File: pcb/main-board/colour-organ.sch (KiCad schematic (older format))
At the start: 39 parts, among them U4 LM358_BIG, U5 LM358_BIG

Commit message: working on finding components for parts
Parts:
- R13: renamed from R19; value 15k -> 18k
- R14: renamed from R23; value 3.9k -> 8.2k
- R15: renamed from R20; value 15k -> 18k
- R16: renamed from R28; value 8.2k -> 18k
- R19: renamed from R24; value 10k -> 2.2k
- R20: renamed from R26; value 680R -> 180R
- R21: renamed from R12; value 15k -> 18k
- R22: renamed from R17; value 10k -> 2.2k
- R23: renamed from R22; value 680R -> 180R
- R24: renamed from R25; value 100k -> 22k
- R25: renamed from R18; value 100k -> 22k
- R26: renamed from R13; value 15k -> 18k
- R29: renamed from R10; value 10k -> 2.2k
- R30: renamed from R14; value 680R -> 180R
- R31: renamed from R11; value 100k -> 22k
- renumbered C25 to C14, C16 to C15, C26 to C16, C20 to C17, C17 to C18, C23 to C19, C24 to C20, C14 to C22, C27 to C23, C19 to C24, C22 to C25, C15 to C26, C18 to C27, D3 to D1, D1 to D3, R9 to R17, R16 to R18, R21 to R28, R15 to R32, U5 to U4, U4 to U5
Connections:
- net at C19.1, R15.2: now also U4.5 (NON_INV); no longer U4.3 (NON_INV)
- net at C17.1, C21.2: now also U4.6 (INV), U4.7 (OUT); no longer U4.1 (OUT), U4.2 (INV)
- net at C20.2, R14.2: now also U4.1 (OUT), U4.2 (INV); no longer U4.6 (INV), U4.7 (OUT)
- net at C16.1, R16.2: now also U4.3 (NON_INV); no longer U4.5 (NON_INV)
- net at R17.2, R21.1: now also U5.1 (OUT), U5.2 (INV); no longer U5.6 (INV), U5.7 (OUT)
- net at C18.1, R18.2: now also U5.3 (NON_INV); no longer U5.5 (NON_INV)
- net at C24.1, R26.2: now also U5.5 (NON_INV); no longer U5.3 (NON_INV)
- net at C22.1, C26.2: now also U5.6 (INV), U5.7 (OUT); no longer U5.1 (OUT), U5.2 (INV)

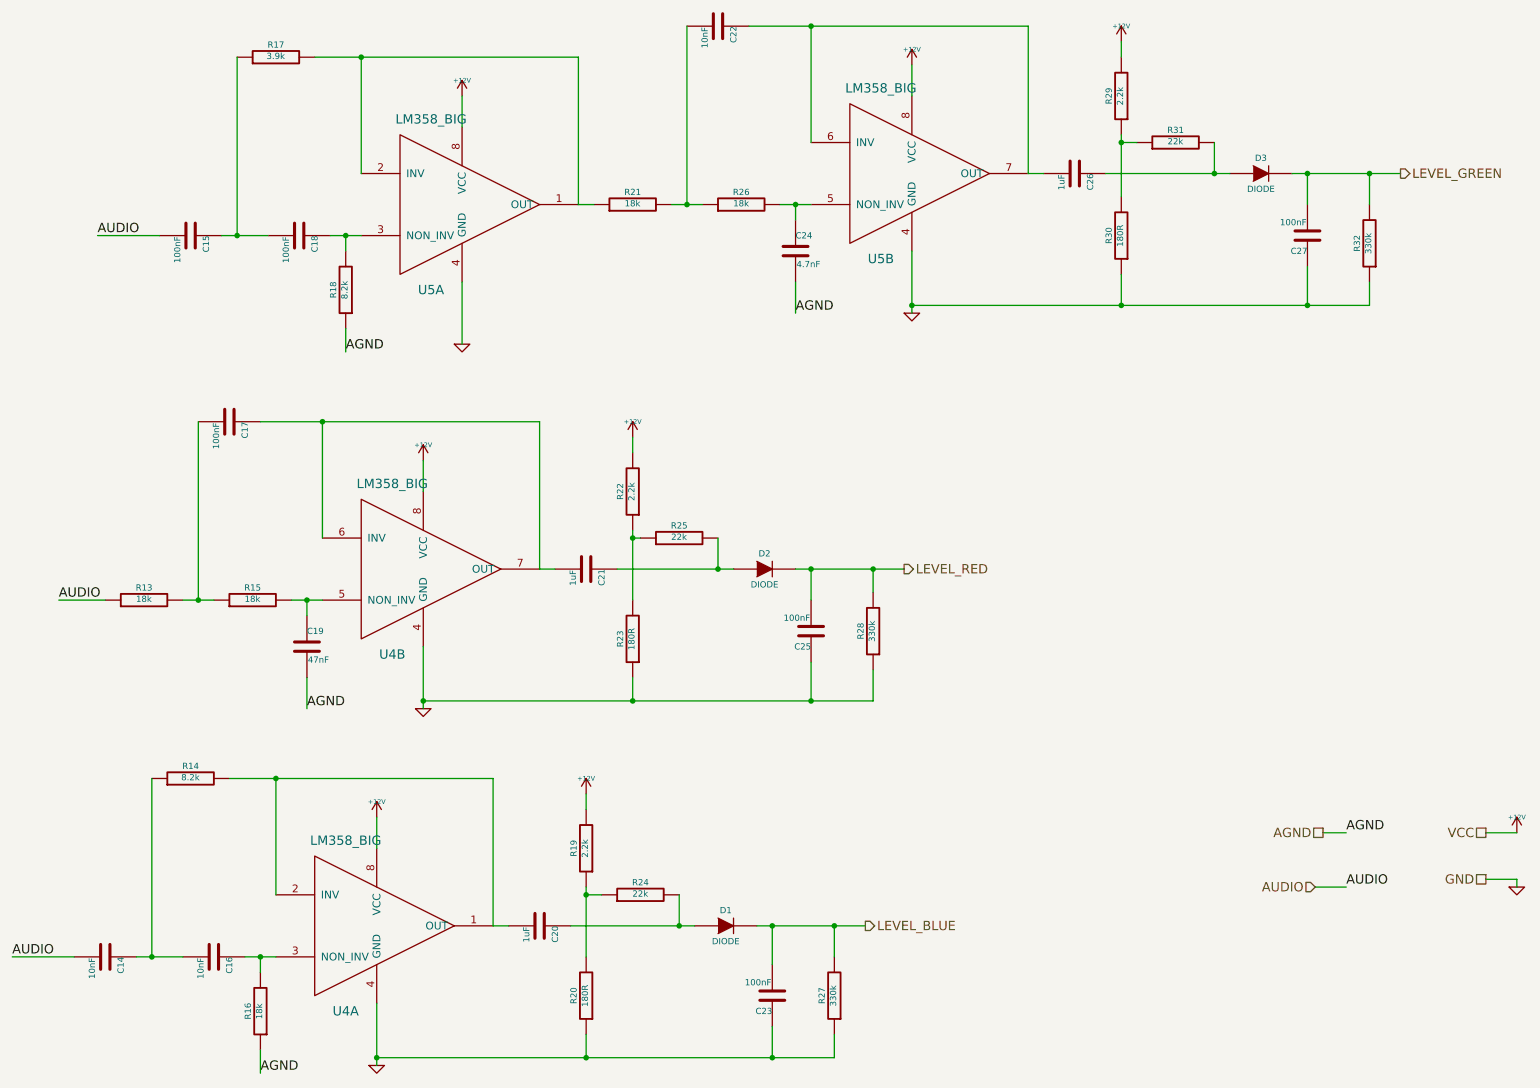
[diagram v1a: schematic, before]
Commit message: finished choosing components for main board
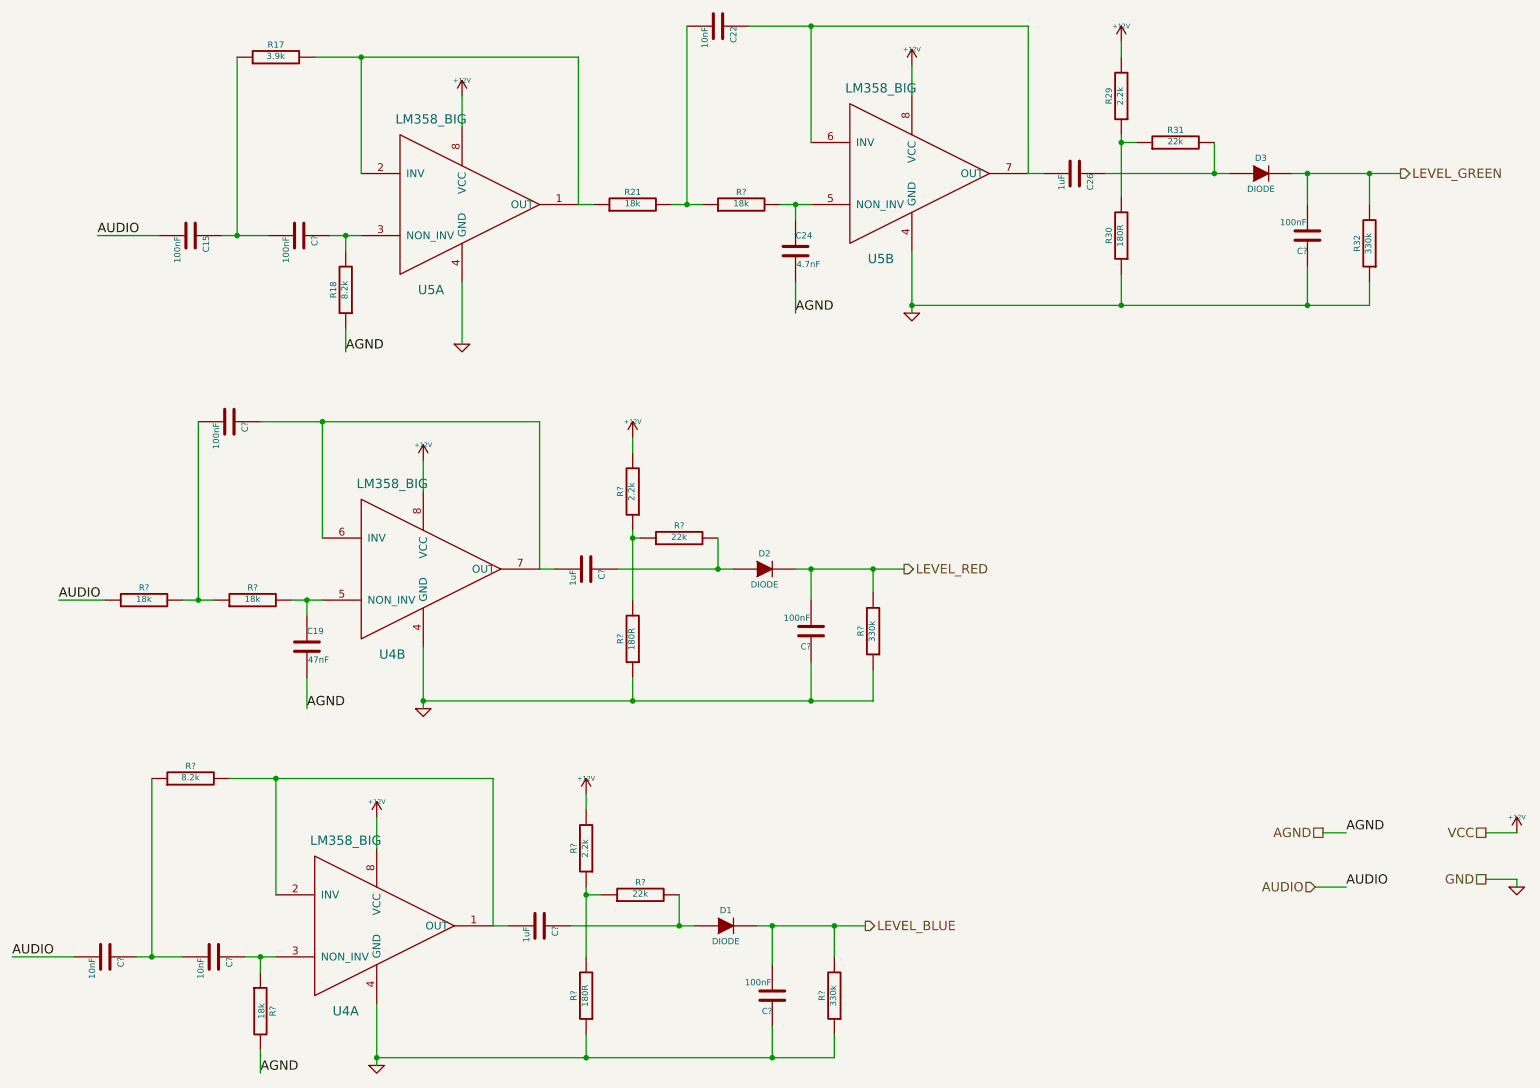
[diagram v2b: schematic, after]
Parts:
- removed C14, C16: 10nF, ~, symbol C-rgb
- removed C17, C18, C23, C25, C27: 100nF, ~, symbol C-rgb
- removed C20, C21: 1uF, ~, symbol C-rgb
- removed R13, R15, R16, R26: 18k, ~, symbol R-rgb
- removed R14: 8.2k, ~, symbol R-rgb
- removed R19, R22: 2.2k, ~, symbol R-rgb
- removed R20, R23: 180R, ~, symbol R-rgb
- removed R24, R25: 22k, ~, symbol R-rgb
- removed R27, R28: 330k, ~, symbol R-rgb
- added C? (x5): 100nF, ~, symbol C-rgb
- added C? (x2): 10nF, ~, symbol C-rgb
- added C? (x2): 1uF, ~, symbol C-rgb
- added R?: 8.2k, ~, symbol R-rgb
- added R? (x4): 18k, ~, symbol R-rgb
- added R? (x2): 2.2k, ~, symbol R-rgb
- added R? (x2): 180R, ~, symbol R-rgb
- added R? (x2): 330k, ~, symbol R-rgb
- added R? (x2): 22k, ~, symbol R-rgb
- C15: Manufacturer Multicomp -> Kemet; Order (none) -> No; Product code MC0805B104K500A2.54MM -> C320C104J5R5TA; Product description Multilayer Ceramic Capacitor, MC Series, 0.1 µF, ± 10%, X7R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 -> 0.10µF 50V Ceramic Capacitor X7R Radial 0.200\" L x 0.125\"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; Supplier Farnell -> Digikey; Supplier URL (none) -> http://www.digikey.co.uk/product-detail/en/kemet/C320C104J5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; Supplier code 2309020 -> 399-9775-ND
- C19: Manufacturer Multicomp -> Kemet; Order (none) -> No; Product code MCRR25473X7RK0050 -> C320C473K5R5TA; Product description Multilayer Ceramic Capacitor, MCRR Series, 0.047 µF, ± 10%,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 -> 0.047µF 50V Ceramic Capacitor X7R Radial 0.200\" L x 0.125\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; Supplier Farnell -> Digikey; Supplier URL (none) -> http://www.digikey.co.uk/product-detail/en/kemet/C320C473K5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; Supplier code 1216437 -> 399-4306-ND
- C22: Manufacturer Multicomp -> Kemet; Order (none) -> No; Product code MCRR25103X7RK0050 -> C315C103J5R5TA; Product description Multilayer Ceramic Capacitor, MCRR Series, 0.01 µF, ± 10%, 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 -> 10000pF 50V Ceramic Capacitor X7R Radial 0.150\" L x 0.100\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; Supplier Farnell -> Digikey; Supplier URL (none) -> http://www.digikey.co.uk/product-detail/en/kemet/C315C103J5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; Supplier code 1216435 -> 399-9712-ND; Tolerance 10% -> 5%
- C24: Order (none) -> No; Product code C315C472K1R5TA -> C320C472J1G5TA; Product description Multilayer Ceramic Capacitor, Gold Max, C315 Series, 4700 p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 -> 4700pF 100V Ceramic Capacitor C0G, NP0 Radial 0.200\" L x 0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; Supplier Farnell -> Digikey; Supplier URL (none) -> http://www.digikey.co.uk/product-search/en/capacitors/ceram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; Supplier code 1457649 -> 399-4302-ND; Tolerance 10% -> 5%
- C26: Manufacturer Multicomp -> Kemet; Notes 5.08mm spacing -> (none); Order (none) -> No; Product code MCMLR50V105KX7R -> C315C105K3R5TA; Product description Multilayer Ceramic Capacitor, MLR Series, 1 µF, ± 10%, X7R,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 -> 1µF 25V Ceramic Capacitor X7R Radial 0.150\" L x 0.100\" W 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; Supplier Farnell -> Digikey; Supplier URL (none) -> http://www.digikey.co.uk/product-search/en/capacitors/ceram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; Supplier code 2112947 -> 399-9714-ND
- R17: Manufacturer (none) -> Stackpole Electronics Inc.; Order (none) -> No; Product code (none) -> CF18JT3K90; Product description (none) -> RES 3.9K OHM 1/8W 5% CARBON FILM; Supplier (none) -> Digikey; Supplier URL (none) -> http://www.digikey.co.uk/product-detail/en/stackpole-electr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; Supplier code (none) -> CF18JT3K90CT-ND
- R18: Manufacturer (none) -> Stackpole Electronics Inc.; Order (none) -> No; Product code (none) -> CF18JT8K20; Product description (none) -> RES 8.2K OHM 1/8W 5% CF AXIAL; Supplier (none) -> Digikey; Supplier URL (none) -> http://www.digikey.co.uk/product-detail/en/stackpole-electr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; Supplier code (none) -> CF18JT8K20CT-ND
- R21: Manufacturer (none) -> Stackpole Electronics Inc.; Order (none) -> No; Product code (none) -> CF18JT18K0; Product description (none) -> RES 18K OHM 1/8W 5% CF AXIAL; Supplier (none) -> Digikey; Supplier URL (none) -> http://www.digikey.co.uk/product-search/en/resistors/throug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; Supplier code (none) -> CF18JT18K0CT-ND
- R29: Manufacturer (none) -> Stackpole Electronics Inc.; Order (none) -> No; Product code (none) -> CF18JT2K20; Product description (none) -> RES 2.2K OHM 1/8W 5% CF AXIAL; Supplier (none) -> Digikey; Supplier URL (none) -> http://www.digikey.co.uk/product-detail/en/stackpole-electr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; Supplier code (none) -> CF18JT2K20CT-ND
- R30: Manufacturer (none) -> Stackpole Electronics Inc.; Order (none) -> No; Product code (none) -> CF18JT180R; Product description (none) -> RES 180 OHM 1/8W 5% CF AXIAL; Supplier (none) -> Digikey; Supplier URL (none) -> http://www.digikey.co.uk/product-detail/en/stackpole-electr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; Supplier code (none) -> CF18JT180RCT-ND
- R31: Manufacturer (none) -> Stackpole Electronics Inc.; Order (none) -> No; Product code (none) -> CF18JT22K0; Product description (none) -> RES 22K OHM 1/8W 5% CF AXIAL; Supplier (none) -> Digikey; Supplier URL (none) -> http://www.digikey.co.uk/product-detail/en/stackpole-electr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; Supplier code (none) -> CF18JT22K0CT-ND
- R32: Manufacturer (none) -> Stackpole Electronics Inc.; Order (none) -> No; Product code (none) -> CF18JT330K; Product description (none) -> RES 330K OHM 1/8W 5% CF AXIAL; Supplier (none) -> Digikey; Supplier URL (none) -> http://www.digikey.co.uk/product-detail/en/stackpole-electr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; Supplier code (none) -> CF18JT330KCT-ND
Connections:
- net +12V: now also R?.2, R?.2
- net AGND: now also R?.2
- net AUDIO: now also C?.2, R?.1
- net GND: now also C?.1, C?.1, C?.1, R?.1, R?.1, R?.1, R?.1
- net LEVEL_BLUE: now also C?.2, R?.2
- net LEVEL_GREEN: now also C?.2
- net LEVEL_RED: now also C?.2, R?.2
- net at C19.1, U4.5 (NON_INV): now also R?.2
- net at U4.6 (INV), U4.7 (OUT): now also C?.1, C?.2
- net at D2.1 (A): now also C?.1, R?.2
- net at U4.1 (OUT), U4.2 (INV): now also C?.2, R?.2
- net at U4.3 (NON_INV): now also C?.1, R?.1
- net at C15.1, R17.1: now also C?.2
- net at R18.2, U5.3 (NON_INV): now also C?.1
- net at C22.2, R21.2: now also R?.1
- net at C24.1, U5.5 (NON_INV): now also R?.2
- net at D1.1 (A): now also C?.1, R?.2
- new net: C?.2, R?.1, R?.2
- new net: C?.1, C?.2, R?.1
- new net: R?.1, R?.1, R?.2 (x2)

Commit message: misc. changes
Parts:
- D1, D2, D3: value DIODE -> DIODE-rgb; footprint ~ -> (none); Manufacturer Multicomp -> Fairchild Semiconductor; Order (none) -> No; Product description Small Signal Diode, Single, 100 V, 150 mA, 1 V, 4 ns, 500 mA -> Diode Standard 100V 200mA Through Hole DO-35; Supplier Farnell -> Digikey; Supplier URL (none) -> http://www.digikey.co.uk/product-detail/en/fairchild-semico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; Supplier code 9565124 -> 1N4148FS-ND
- U4, U5: Manufacturer (none) -> Texas Instruments; Order (none) -> No; Product code (none) -> LM358P; Product description (none) -> General Purpose Amplifier 2 Circuit 8-PDIP; Supplier (none) -> Digikey; Supplier URL (none) -> http://www.digikey.co.uk/product-detail/en/texas-instrument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; Supplier code (none) -> 296-1395-5-ND
- gave numbers to parts that had none: 22
